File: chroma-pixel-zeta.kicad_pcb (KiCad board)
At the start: 6 copper layers, 76 x 78 mm, 134 parts, among them J1 Micro_SD_Card_Det_Hirose_DM3AT, J10 Conn_01x06_MountingPin, J2 TFT_LCD, J4 USB-C, J5 I2C-STEMMA-QT, J6 BAT, J7 swd, J8 SPKR, J9 UART, SW1 SW_Push, SW2 SW_Push, SW3 SW_Push, SW4 SW_Push, U1 MT25Q, U10 STM32H743ZITx, U11 MT48LC16M16A2P, U5 TPS61169, U6 MAX98357AETE_, U7 CAT24C128, U8 TLV75733PDBV, Y1 25MHz, Y2 32.768KHz

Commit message: Change MCU to STM32H743IIT6
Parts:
- removed U10: STM32H743ZITx, Package_QFP:LQFP-144_20x20mm_P0.5mm
- added U2: STM32H743IITx, Package_QFP:LQFP-176_24x24mm_P0.5mm, F.Cu at (209.2, 83.5)
- moved C10 83.2 mm to (68.8, 75.6)
- moved C21 83.2 mm to (90.7, 86.8)
- moved C24 83.2 mm to (31.8, 99.3)
- moved C27 83.2 mm to (31.8, 110.9)
- moved C28 83.2 mm to (31.8, 116.6)
- moved C29 83.2 mm to (46.1, 80.6)
- moved C35 83.2 mm to (75.8, 104.1)
- moved C42 83.2 mm to (73.4, 73.5)
- moved D5 83.2 mm to (86.2, 51.6)
- moved D6 83.2 mm to (79.2, 51.6)
- moved H2 83.2 mm to (95.6, 52.7)
- moved H3 83.2 mm to (95.6, 123.9)
- moved J10 83.2 mm to (58.1, 52.9)
- moved J2 83.2 mm to (68.5, 36.9)
- moved J5 83.2 mm to (58.0, 122.0)
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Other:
- board size 76 x 78 mm -> 244.9 x 78 mm

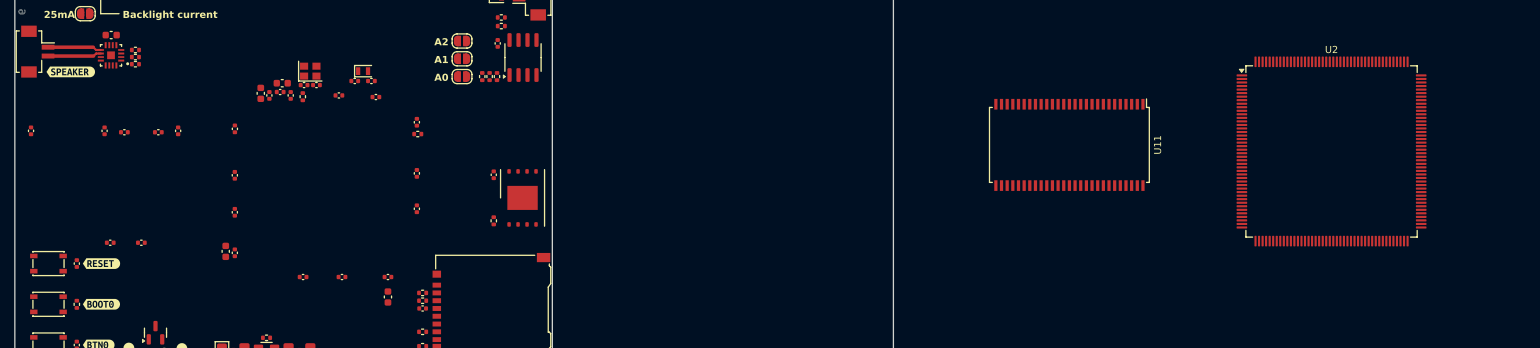
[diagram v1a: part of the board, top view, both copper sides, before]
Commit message: Cleaning schematic, added more independently schematics
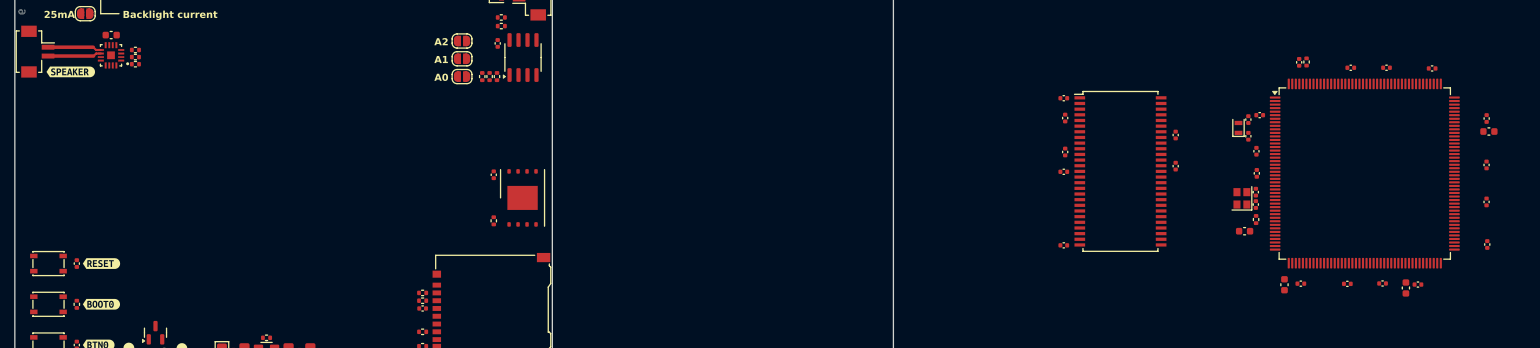
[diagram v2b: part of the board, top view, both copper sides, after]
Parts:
- moved C34 179.4 mm to (231.4, 80.7), turned to 0 degrees
- moved C14 177.0 mm to (231.1, 78.8), turned to -90 degrees
- moved C15 177.0 mm to (231.1, 85.4), turned to -90 degrees
- moved C16 177.0 mm to (231.1, 90.6), turned to -90 degrees
- moved C25 172.0 mm to (231.2, 96.6), turned to -90 degrees
- moved C9 161.6 mm to (221.4, 102.3), turned to 180 degrees
- moved C37 151.0 mm to (187.2, 85.6), turned to -90 degrees
- moved C19 147.3 mm to (202.5, 102.3), turned to -90 degrees
- moved C38 147.0 mm to (187.2, 81.2), turned to -90 degrees
- moved C1 146.9 mm to (171.3, 96.8), turned to 180 degrees
- moved C17 145.2 mm to (198.6, 83.5)
- moved C8 144.9 mm to (223.4, 71.8), turned to 0 degrees
- moved C35 143.9 mm to (219.7, 102.8)
- moved C6 142.2 mm to (211.4, 102.2)
- moved C5 141.1 mm to (204.9, 102.2)
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
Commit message: Layout SDRAM
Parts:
- removed U11: MT48LC16M16A2P, Package_SO:TSOP-II-54_22.2x10.16mm_P0.8mm
- removed kibuzzard-66417165: G***, kibuzzard-66417165
- removed kibuzzard-66417197: G***, kibuzzard-66417197
- removed kibuzzard-6641D19D: G***, kibuzzard-6641D19D
- removed kibuzzard-6641D1A5: G***, kibuzzard-6641D1A5
- removed kibuzzard-6641D1AA: G***, kibuzzard-6641D1AA
- removed kibuzzard-6641D1B0: G***, kibuzzard-6641D1B0
- removed kibuzzard-6642BE54: G***, kibuzzard-6642BE54
- removed kibuzzard-6642BE6C: G***, kibuzzard-6642BE6C
- removed kibuzzard-6642BE85: G***, kibuzzard-6642BE85
- removed kibuzzard-664329E8: G***, kibuzzard-664329E8
- removed kibuzzard-664329F6: G***, kibuzzard-664329F6
- removed kibuzzard-6644A0DC: G***, kibuzzard-6644A0DC
- removed kibuzzard-6644A120: G***, kibuzzard-6644A120
- removed kibuzzard-6644A126: G***, kibuzzard-6644A126
- added C22: 100n, Capacitor_SMD:C_0402_1005Metric, F.Cu at (181.1, 97.6)
- added J3: Conn_01x10_MountingPin, Connector_FFC-FPC:Hirose_FH12-10S-0.5SH_1x10-1MP_P0.50mm_Horizontal, F.Cu at (120.4, 148.3)
- added R1: 10K, Resistor_SMD:R_0402_1005Metric, F.Cu at (181.1, 91.6)
- added R35: 4K7, Resistor_SMD:R_0402_1005Metric, F.Cu at (133.1, 142.4)
- added R36: 4K7, Resistor_SMD:R_0402_1005Metric, F.Cu at (133.1, 144.4)
- added U10: PCM5102A, Package_SO:TSSOP-20_4.4x6.5mm_P0.65mm, F.Cu at (199.6, 98.7)
- added U4: MT25Q, Package_SON:WSON-8-1EP_8x6mm_P1.27mm_EP3.4x4.3mm, F.Cu at (174.8, 102.0)
- added U9: MT48LC16M16A2P, Package_SO:TSOP-II-54_22.2x10.16mm_P0.8mm, F.Cu at (142.3, 128.5)
- J10: value Conn_01x06_MountingPin -> Conn_01x24_MountingPin; footprint Connector_FFC-FPC:TE_84953-6_1x06-1MP_P1.0mm_Horizontal -> Connector_FFC-FPC:Hirose_FH12-24S-0.5SH_1x24-1MP_P0.50mm_Horizontal
- R31, R32: value 10K -> 2K2
- R5, R6: value 2K2 -> 10K
- moved SW1 207.1 mm to (231.6, 62.6), turned to 90 degrees
- moved SW2 206.6 mm to (231.6, 71.6), turned to 90 degrees
- moved SW3 206.1 mm to (231.6, 80.6), turned to 90 degrees
- moved SW4 205.6 mm to (231.6, 89.6), turned to 90 degrees
- moved H1 203.7 mm to (229.8, 40.9)
- moved C24 193.1 mm to (222.1, 66.4)
- moved C27 193.1 mm to (222.1, 78.0)
- moved C28 193.1 mm to (222.1, 83.7)
- moved R18 193.1 mm to (222.1, 72.2)
- moved H2 164.8 mm to (228.9, 149.5)
- moved J9 158.7 mm to (171.9, 39.8), turned to 180 degrees
- moved D7 153.3 mm to (219.6, 144.5), turned to 90 degrees
- moved JP1 153.3 mm to (164.8, 142.2), turned to 180 degrees
- moved JP2 153.1 mm to (164.8, 138.6), turned to 180 degrees
- moved JP3 153.0 mm to (164.8, 135.1), turned to 180 degrees
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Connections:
- net /Audio/GAIN_SLOT renamed /AUDIO/GAIN_SLOT
- net /Audio/SPK+ renamed /AUDIO/SPK+
- net /Audio/SPK- renamed /AUDIO/SPK-
- net /IO/NRST renamed /MCU/NRST
- net /IO/SWCLK renamed /IO/DBG_SWCLK
- net /IO/SWDIO renamed /IO/DBG_SWDIO
- net /IO/USART1_RX renamed /IO/DBG_RX
- net /IO/USART1_TX renamed /IO/DBG_TX
- net /LCD/HSYNC renamed /LCD/LTDC_HSYNC
- net /LCD/LCD_CLK renamed /LCD/LTDC_CLK
- net /LCD/LCD_DE renamed /LCD/LTDC_DE
- net /LCD/LCD_SPI_CS renamed /LCD/LCD_CS
- net /LCD/VSYNC renamed /LCD/LTDC_VSYNC
- net /MCU/I2S_CK renamed /AUDIO/I2S_CK
- net /MCU/I2S_SDO renamed /AUDIO/I2S_SDO
- net /MCU/I2S_SD_MODE renamed /AUDIO/I2S_SD_MODE
- net /MCU/I2S_WS renamed /AUDIO/I2S_WS
- net /MCU/SD_CLK renamed /MEMORY SD CARD/SD_CLK
- net /MCU/SD_CMD renamed /MEMORY SD CARD/SD_CMD
- net /MCU/SD_DAT0 renamed /MEMORY SD CARD/SD_DAT0
- net /MCU/SD_DAT1 renamed /MEMORY SD CARD/SD_DAT1
- net /MCU/SD_DAT2 renamed /MEMORY SD CARD/SD_DAT2
- net /MCU/SD_DAT3 renamed /MEMORY SD CARD/SD_DAT3
- net /MCU/SHIELD renamed /USB/SHIELD
- net /MCU/USB_D+ renamed /USB/USB_D+
- net /MCU/USB_D- renamed /USB/USB_D-
- J1 pad 9: /MCU/PG13 -> /MEMORY SD CARD/SD_DET
- J10 pad 1: GND -> unconnected-(J10-Pin_1-Pad1)
- J10 pad 2: /LCD/LCD_TP_INT -> unconnected-(J10-Pin_2-Pad2)
- J10 pad 3: /LCD/LCD_TP_RST -> unconnected-(J10-Pin_3-Pad3)
- J10 pad 4: +3V3 -> unconnected-(J10-Pin_4-Pad4)
- J10 pad 5: /LCD/LCD_TP_SCL -> unconnected-(J10-Pin_5-Pad5)
- J10 pad 6: /LCD/LCD_TP_SDA -> unconnected-(J10-Pin_6-Pad6)
- J2 pad 5: /LCD/LCD_SPI_DAT -> /LCD/LCD_SDA
- J2 pad 6: /LCD/LCD_SPI_CLK -> /LCD/LCD_SCL
- J7 pad 8: unconnected-(J7-Pin_8-Pad8) -> /IO/DBG_SWO
- R10 pad 1: /MCU/PG13 -> +3V3
- R10 pad 2: +3V3 -> /MEMORY SD CARD/SD_DET
- R2 pad 2: /MCU/~{NOR_CS} -> /MCU/QUADSPI_BK2_NCS
- R31 pad 1: Net-(JP6-A) -> +3V3
- R31 pad 2: GND -> /MEMORY EEPROM/SDA
- R32 pad 1: Net-(JP5-A) -> +3V3
- R32 pad 2: GND -> /MEMORY EEPROM/SCL
- R33 pad 2: /LCD/LCD_TP_SDA -> /LCD/LCD_TP_SCL
- R34 pad 2: /LCD/LCD_TP_SCL -> /LCD/LCD_TP_SDA
- R5 pad 1: +3V3 -> Net-(JP5-A)
- R5 pad 2: /IO/STEMMA_SCL -> GND
- R6 pad 1: +3V3 -> Net-(JP6-A)
- R6 pad 2: /IO/STEMMA_SDA -> GND
- U1 pad 1: /MCU/~{NOR_CS} -> /MCU/QUADSPI_BK1_NCS
- U1 pad 2: /MCU/NOR_D1 -> /MCU/QUADSPI_BK1_IO1
- U1 pad 3: /MCU/NOR_D2 -> /MCU/QUADSPI_BK1_IO2
- U1 pad 5: /MCU/NOR_D0 -> /MCU/QUADSPI_BK1_IO0
- U1 pad 6: /MCU/NOR_CLK -> /MCU/QUADSPI_CLK
- U1 pad 7: /MCU/NOR_D3 -> /MCU/QUADSPI_BK1_IO3
- U2 pad 104: unconnected-(U2-PD14-Pad104) -> /MCU/SDRAM_DQ0
- U2 pad 105: unconnected-(U2-PD15-Pad105) -> /MCU/SDRAM_DQ1
- U2 pad 106: unconnected-(U2-PG2-Pad106) -> /MCU/SDRAM_ADD12
- U2 pad 108: unconnected-(U2-PG4-Pad108) -> /MEMORY SDRAM/SDRAM_BA0
- U2 pad 109: unconnected-(U2-PG5-Pad109) -> /MEMORY SDRAM/SDRAM_BA1
- U2 pad 112: unconnected-(U2-PG8-Pad112) -> /MEMORY SDRAM/SDRAM_CLK
- U2 pad 140: unconnected-(U2-PC11-Pad140) -> /MCU/QUADSPI_BK2_NCS
- U2 pad 142: unconnected-(U2-PD0-Pad142) -> /MCU/SDRAM_DQ2
- U2 pad 143: unconnected-(U2-PD1-Pad143) -> /MCU/SDRAM_DQ3
- U2 pad 152: unconnected-(U2-PG9-Pad152) -> /MCU/QUADSPI_BK2_IO2
- U2 pad 157: unconnected-(U2-PG14-Pad157) -> /MCU/QUADSPI_BK2_IO3
- U2 pad 16: unconnected-(U2-PF0-Pad16) -> /MCU/SDRAM_ADD0
- U2 pad 160: unconnected-(U2-PG15-Pad160) -> /MEMORY SDRAM/~{SDRAM_CAS}
- U2 pad 161: unconnected-(U2-PB3-Pad161) -> /IO/DBG_SWO
- U2 pad 169: unconnected-(U2-PE0-Pad169) -> /MEMORY SDRAM/SDRAM_LDQM
- U2 pad 17: unconnected-(U2-PF1-Pad17) -> /MCU/SDRAM_ADD1
- U2 pad 170: unconnected-(U2-PE1-Pad170) -> /MEMORY SDRAM/SDRAM_UDQM
- U2 pad 18: unconnected-(U2-PF2-Pad18) -> /MCU/SDRAM_ADD2
- U2 pad 19: unconnected-(U2-PF3-Pad19) -> /MCU/SDRAM_ADD3
- U2 pad 20: unconnected-(U2-PF4-Pad20) -> /MCU/SDRAM_ADD4
- U2 pad 21: unconnected-(U2-PF5-Pad21) -> /MCU/SDRAM_ADD5
- U2 pad 24: unconnected-(U2-PF6-Pad24) -> /MCU/QUADSPI_BK1_IO3
- U2 pad 25: unconnected-(U2-PF7-Pad25) -> /MCU/QUADSPI_BK1_IO2
- U2 pad 26: unconnected-(U2-PF8-Pad26) -> /MCU/QUADSPI_BK1_IO0
- U2 pad 27: unconnected-(U2-PF9-Pad27) -> /MCU/QUADSPI_BK1_IO1
- U2 pad 35: unconnected-(U2-PC3_C-Pad35) -> /MEMORY SDRAM/SDRAM_CKE
- U2 pad 43: unconnected-(U2-PH2-Pad43) -> /MCU/QUADSPI_BK2_IO0
- U2 pad 44: unconnected-(U2-PH3-Pad44) -> /MCU/QUADSPI_BK2_IO1
- U2 pad 53: unconnected-(U2-PA7-Pad53) -> /MEMORY SDRAM/~{SDRAM_WE}
- U2 pad 54: unconnected-(U2-PC4-Pad54) -> /MEMORY SDRAM/~{SDRAM_CS}
- U2 pad 58: unconnected-(U2-PB2-Pad58) -> /MCU/QUADSPI_CLK
- U2 pad 59: unconnected-(U2-PF11-Pad59) -> /MEMORY SDRAM/~{SDRAM_RAS}
- U2 pad 60: unconnected-(U2-PF12-Pad60) -> /MCU/SDRAM_ADD6
- U2 pad 63: unconnected-(U2-PF13-Pad63) -> /MCU/SDRAM_ADD7
- U2 pad 64: unconnected-(U2-PF14-Pad64) -> /MCU/SDRAM_ADD8
- U2 pad 65: unconnected-(U2-PF15-Pad65) -> /MCU/SDRAM_ADD9
- U2 pad 66: unconnected-(U2-PG0-Pad66) -> /MCU/SDRAM_ADD10
- U2 pad 67: unconnected-(U2-PG1-Pad67) -> /MCU/SDRAM_ADD11
- U2 pad 68: unconnected-(U2-PE7-Pad68) -> /MCU/SDRAM_DQ4
- U2 pad 69: unconnected-(U2-PE8-Pad69) -> /MCU/SDRAM_DQ5
- U2 pad 70: unconnected-(U2-PE9-Pad70) -> /MCU/SDRAM_DQ6
- U2 pad 73: unconnected-(U2-PE10-Pad73) -> /MCU/SDRAM_DQ7
- U2 pad 74: unconnected-(U2-PE11-Pad74) -> /MCU/SDRAM_DQ8
- U2 pad 75: unconnected-(U2-PE12-Pad75) -> /MCU/SDRAM_DQ9
- U2 pad 76: unconnected-(U2-PE13-Pad76) -> /MCU/SDRAM_DQ10
- U2 pad 77: unconnected-(U2-PE14-Pad77) -> /MCU/SDRAM_DQ11
- U2 pad 78: unconnected-(U2-PE15-Pad78) -> /MCU/SDRAM_DQ12
- U2 pad 79: unconnected-(U2-PB10-Pad79) -> /MCU/QUADSPI_BK1_NCS
- U2 pad 96: unconnected-(U2-PD8-Pad96) -> /MCU/SDRAM_DQ13
- U2 pad 97: unconnected-(U2-PD9-Pad97) -> /MCU/SDRAM_DQ14
- U2 pad 98: unconnected-(U2-PD10-Pad98) -> /MCU/SDRAM_DQ15
- U7 pad 1: Net-(JP7-A) -> Net-(JP5-A)
- U7 pad 3: Net-(JP5-A) -> Net-(JP7-A)
- U7 pad 5: /IO/STEMMA_SCL -> /MEMORY EEPROM/SDA
- U7 pad 6: /IO/STEMMA_SDA -> /MEMORY EEPROM/SCL
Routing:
- net +3V3: track 0.00 -> 83.4 mm, vias 0 -> 4
- net GND: track 0.00 -> 65.7 mm, vias 0 -> 5
- net Net-(C34-Pad1): track 0.00 -> 8.60 mm
- net /AUDIO/SPK+: track 7.63 -> 0.00 mm
- net /AUDIO/SPK-: track 7.61 -> 0.00 mm
- net Net-(U2-PDR_ON): track 0.00 -> 4.23 mm
- net VBAT: track 0.00 -> 4.00 mm
- removed copper zone on F.Cu, net /USB/SHIELD
- removed copper zone on In4.Cu, net GND
- removed copper zone on F.Cu, net VBUS
- removed copper zone on In2.Cu, net VBUS
- removed copper zone on F.Cu, net VDD
- removed copper zone on In3.Cu, net VDD
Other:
- board size 244.9 x 78 mm -> 183.4 x 116.6 mm
- copper layers 6 -> 4
- board text removed: "1"
- board text removed: "100mA"
- board text removed: "2"
- board text removed: "25mA"
- board text removed: "3"
- board text removed: "4"
- board text removed: "40"
- board text removed: "5"
- board text removed: "50mA"
- board text removed: "6"
- board text removed: "A0"
- board text removed: "A1"
- board text removed: "A2"
- board text removed: "Backlight current"

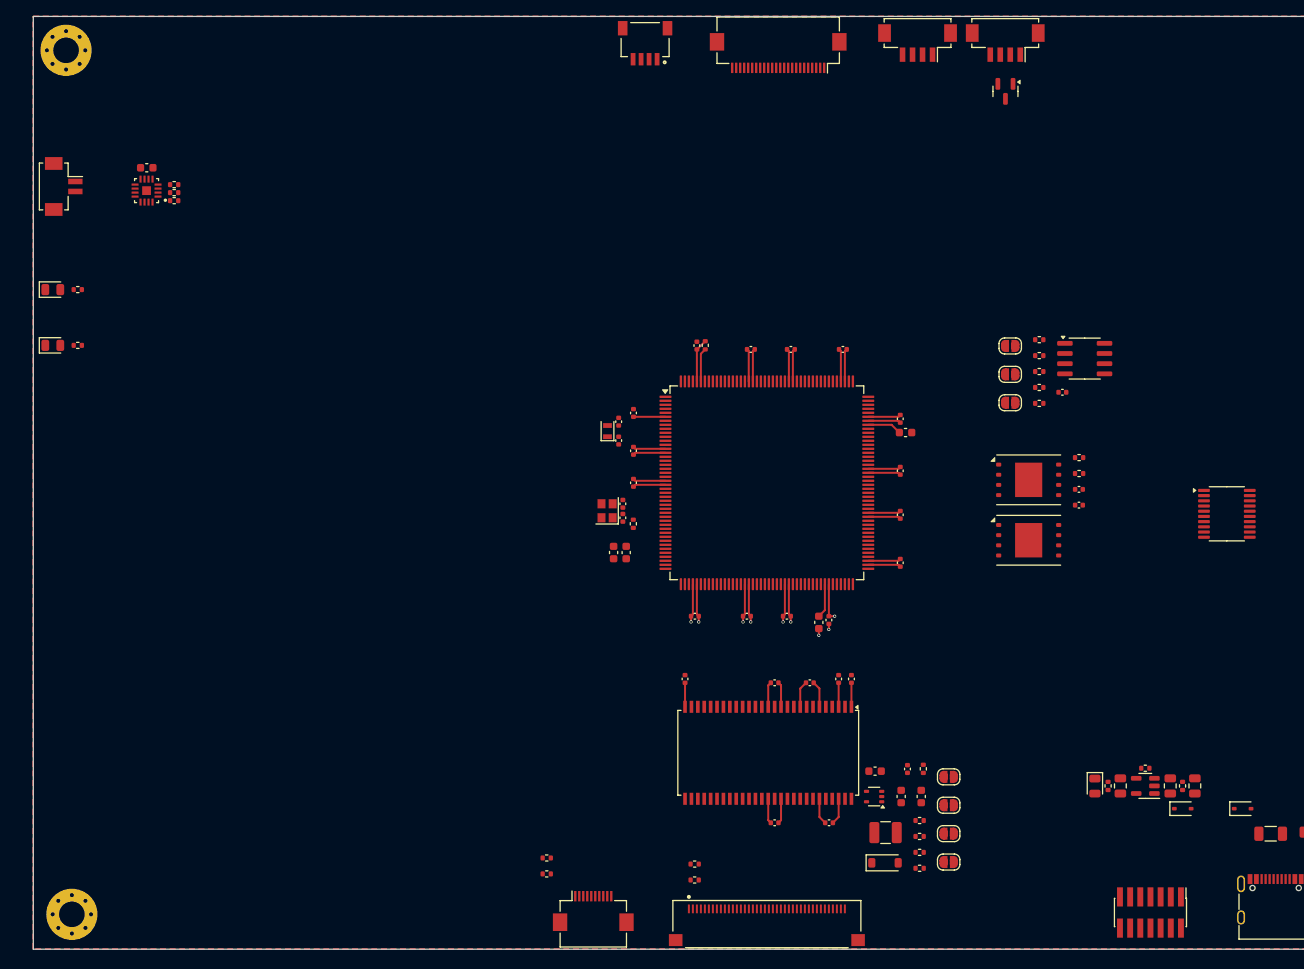
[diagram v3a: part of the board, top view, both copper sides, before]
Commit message: relayout SDRAM
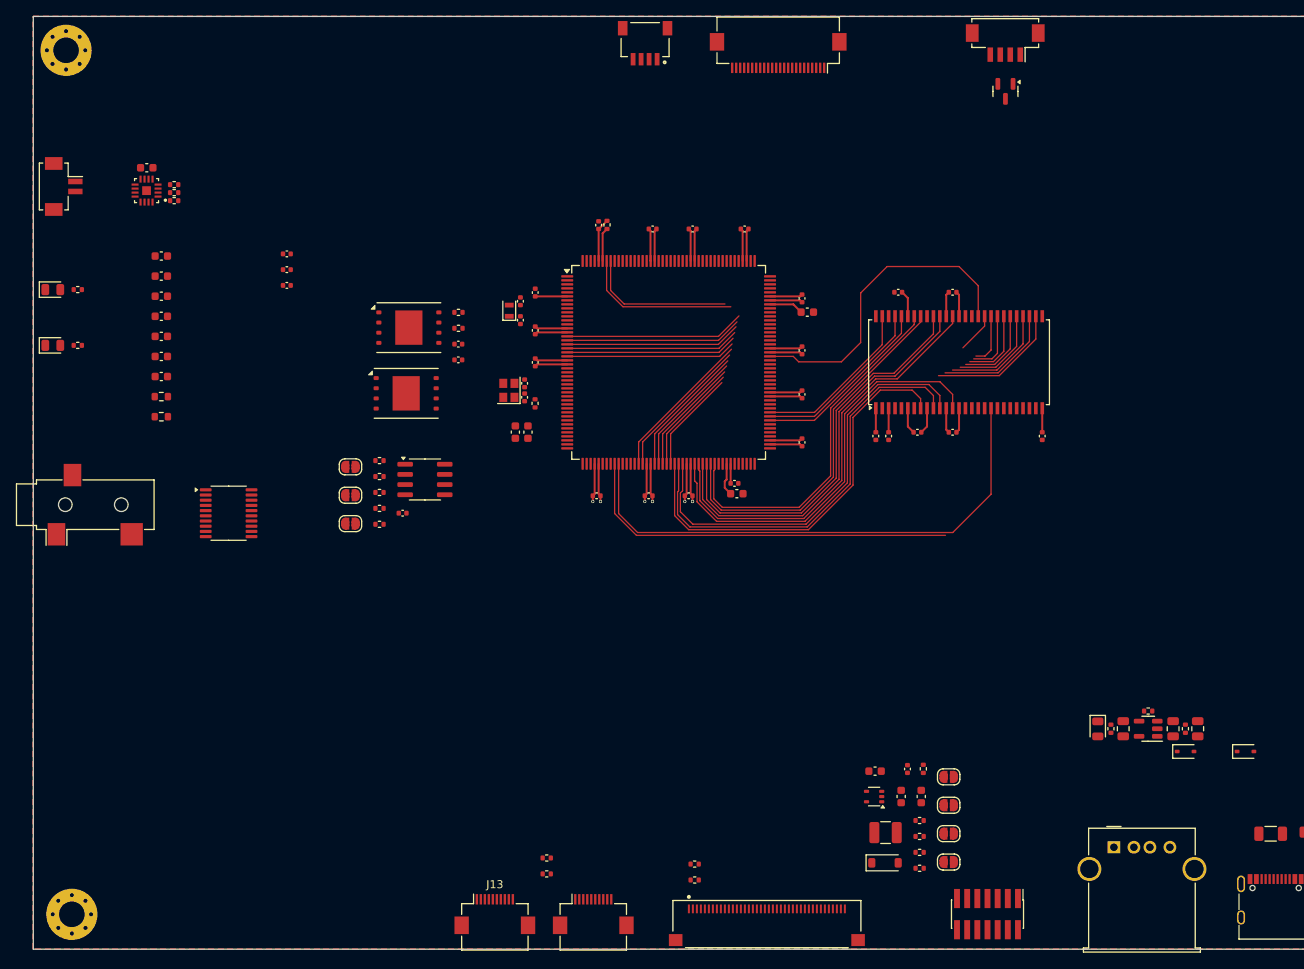
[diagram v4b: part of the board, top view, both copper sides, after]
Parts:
- removed the J9 at (160.9, 39.8)
- added C50: 2.2u, Capacitor_SMD:C_0603_1608Metric, F.Cu at (66.4, 66.4)
- added C51: 2.2u, Capacitor_SMD:C_0603_1608Metric, F.Cu at (66.4, 68.9)
- added C52: 2.2u, Capacitor_SMD:C_0603_1608Metric, F.Cu at (66.4, 71.5)
- added C53: 2.2u, Capacitor_SMD:C_0603_1608Metric, F.Cu at (66.4, 74.0)
- added C54: 10u, Capacitor_SMD:C_0603_1608Metric, F.Cu at (66.4, 76.5)
- added C55: 100n, Capacitor_SMD:C_0402_1005Metric, F.Cu at (82.1, 66.2)
- added C56: 10u, Capacitor_SMD:C_0603_1608Metric, F.Cu at (66.4, 79.0)
- added C57: 100n, Capacitor_SMD:C_0402_1005Metric, F.Cu at (82.1, 68.1)
- added C58: 10u, Capacitor_SMD:C_0603_1608Metric, F.Cu at (66.4, 81.5)
- added C59: 100n, Capacitor_SMD:C_0402_1005Metric, F.Cu at (82.1, 70.1)
- added J11: AudioJack3, Connector_Audio:Jack_3.5mm_CUI_SJ-3523-SMT_Horizontal, F.Cu at (56.9, 97.5)
- added J12: USB_A, Connector_USB:USB_A_Molex_67643_Horizontal, F.Cu at (185.5, 140.3)
- added J13: Conn_01x10_MountingPin, Connector_FFC-FPC:Hirose_FH12-10S-0.5SH_1x10-1MP_P0.50mm_Horizontal, F.Cu at (108.1, 148.7)
- added R37: 470, Resistor_SMD:R_0603_1608Metric, F.Cu at (66.4, 84.0)
- added R38: 470, Resistor_SMD:R_0603_1608Metric, F.Cu at (66.4, 86.5)
- moved U10 124.8 mm to (74.8, 98.6)
- moved C20 83.8 mm to (96.6, 98.6)
- moved JP5 83.8 mm to (90.0, 92.8)
- moved JP6 83.8 mm to (90.0, 96.3)
- moved JP7 83.8 mm to (90.0, 99.9)
- moved R30 83.8 mm to (93.7, 96.0)
- moved R31 83.8 mm to (93.7, 98.0)
- moved R32 83.8 mm to (93.7, 100.0)
- moved R5 83.8 mm to (93.7, 92.0)
- moved R6 83.8 mm to (93.7, 94.0)
- moved U7 83.8 mm to (99.4, 94.4)
- moved U4 81.9 mm to (97.3, 75.4)
- moved C21 79.7 mm to (103.5, 77.4)
- moved C22 79.7 mm to (103.5, 79.4)
- moved R1 79.7 mm to (103.5, 73.5)
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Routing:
- net /MEMORY SDRAM/~{SDRAM_CS}: track 0.00 -> 66.5 mm
- net /MCU/SDRAM_DQ6: track 0.00 -> 53.5 mm
- net /MCU/SDRAM_DQ5: track 0.00 -> 53.2 mm
- net /MCU/SDRAM_DQ8: track 0.00 -> 53.2 mm
- net /MCU/SDRAM_DQ7: track 0.00 -> 52.4 mm
- net /MCU/SDRAM_DQ4: track 0.00 -> 51.8 mm
- net /MCU/SDRAM_DQ9: track 0.00 -> 51.3 mm
- net /MCU/SDRAM_DQ10: track 0.00 -> 49.9 mm
- net /MEMORY SDRAM/~{SDRAM_WE}: track 0.00 -> 48.7 mm
- net /MCU/SDRAM_DQ11: track 0.00 -> 46.7 mm
- net /MCU/SDRAM_DQ12: track 0.00 -> 45.4 mm
- net /MEMORY SDRAM/SDRAM_CLK: track 0.00 -> 39.7 mm
- net /MCU/SDRAM_ADD4: track 0.00 -> 38.4 mm
- net /MCU/SDRAM_ADD5: track 0.00 -> 36.6 mm
- net /MCU/SDRAM_ADD6: track 0.00 -> 31.7 mm
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
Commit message: Finished SDRAM, QSPI Flash, Planning to move to 5 inch orient display dimension
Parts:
- removed J13, J3: Conn_01x10_MountingPin, Connector_FFC-FPC:Hirose_FH12-10S-0.5SH_1x10-1MP_P0.50mm_Horizontal
- added BT1: Battery_Cell, Battery:BatteryHolder_Keystone_2998_1x6.8mm, F.Cu at (66.9, 123.5)
- added C60: 10uF/0805, Capacitor_SMD:C_0805_2012Metric, F.Cu at (188.4, 111.4)
- added C61: 1uF/0805, Capacitor_SMD:C_0805_2012Metric, F.Cu at (188.4, 114.4)
- added C62: 2.2u, Capacitor_SMD:C_0805_2012Metric, F.Cu at (188.4, 117.4)
- added D11: NSR0320MW2T1G, Diode_SMD:D_SOD-323, F.Cu at (195.7, 119.0)
- added D12: GREEN, LED_SMD:LED_0805_2012Metric, F.Cu at (195.7, 116.0)
- added J14: LCD_TP_I2C, Connector_FFC-FPC:TE_84952-6_1x06-1MP_P1.0mm_Horizontal, F.Cu at (110.1, 149.9)
- added J15: LCD_SPI, Connector_FFC-FPC:TE_84952-6_1x06-1MP_P1.0mm_Horizontal, F.Cu at (70.1, 147.5)
- added R39: 100K, Resistor_SMD:R_0402_1005Metric, F.Cu at (192.0, 115.5)
- added R40: 10K, Resistor_SMD:R_0402_1005Metric, F.Cu at (192.0, 117.5)
- added R41: 2K2, Resistor_SMD:R_0402_1005Metric, F.Cu at (192.0, 119.5)
- added U11: TLV75733PDBV, Package_TO_SOT_SMD:SOT-23-5, F.Cu at (193.2, 112.3)
- C50, C51, C52, C53: footprint Capacitor_SMD:C_0603_1608Metric -> Capacitor_SMD:C_0805_2012Metric
- moved H3 409.5 mm to (451.1, 142.5), turned to 0 degrees
- moved H4 406.5 mm to (451.1, 56.5), turned to 90 degrees
- moved C16 255.4 mm to (401.4, 98.6)
- moved C1 255.4 mm to (431.5, 103.5)
- moved C13 255.4 mm to (387.8, 77.6)
- moved C14 255.4 mm to (401.4, 86.3)
- moved C15 255.4 mm to (401.4, 92.8)
- moved C2 255.4 mm to (420.3, 103.1)
- moved C25 255.4 mm to (401.4, 104.3)
- moved C26 255.4 mm to (367.2, 103.0)
- moved C29 255.4 mm to (412.3, 103.5)
- moved C36 255.4 mm to (420.3, 85.6)
- moved C37 255.4 mm to (413.5, 85.6)
- moved C5 255.4 mm to (387.3, 111.0)
- moved C8 255.4 mm to (394.3, 77.6)
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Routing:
- net /MEMORY SDRAM/~{SDRAM_CAS}: track 0.00 -> 56.2 mm, vias 0 -> 2
- net /MEMORY SDRAM/SDRAM_CKE: track 5.07 -> 59.9 mm, vias 0 -> 2
- net /MCU/QUADSPI_BK2_IO2: track 0.00 -> 50.5 mm
- net /MCU/QUADSPI_BK2_IO0: track 0.00 -> 47.2 mm
- net /MCU/QUADSPI_BK2_IO3: track 0.00 -> 46.8 mm
- net /MEMORY SDRAM/SDRAM_LDQM: track 18.7 -> 64.8 mm, vias 0 -> 2
- net /MCU/SDRAM_DQ3: track 0.00 -> 44.4 mm, vias 0 -> 2
- net /MCU/SDRAM_DQ2: track 0.00 -> 42.0 mm, vias 0 -> 2
- net /MCU/QUADSPI_BK2_IO1: track 0.00 -> 42.0 mm
- net /MCU/QUADSPI_CLK: track 0.00 -> 41.6 mm, vias 0 -> 2
- net /MCU/SDRAM_ADD3: track 21.8 -> 62.2 mm, vias 0 -> 2
- net /MCU/SDRAM_ADD10: track 13.8 -> 53.5 mm, vias 0 -> 2
- net /MCU/SDRAM_ADD2: track 22.0 -> 61.6 mm, vias 0 -> 2
- net /MCU/SDRAM_ADD1: track 22.2 -> 61.0 mm, vias 0 -> 2
- net /MCU/SDRAM_ADD0: track 22.5 -> 60.4 mm, vias 0 -> 2
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- added copper zone on B.Cu, net GND
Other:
- board size 183.4 x 116.6 mm -> 292.9 x 116.6 mm

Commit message: Move to 5 inch dimension
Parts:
- moved C1 238.4 mm to (193.3, 93.0)
- moved C10 238.4 mm to (137.9, 66.6)
- moved C12 238.4 mm to (144.6, 67.1)
- moved C13 238.4 mm to (149.6, 67.1)
- moved C14 238.4 mm to (163.3, 75.8)
- moved C15 238.4 mm to (163.3, 82.3)
- moved C16 238.4 mm to (163.3, 88.0)
- moved C2 238.4 mm to (182.1, 92.5)
- moved C25 238.4 mm to (163.3, 93.8)
- moved C26 238.4 mm to (129.0, 92.5)
- moved C29 238.4 mm to (174.1, 93.0)
- moved C36 238.4 mm to (182.1, 75.0)
- moved C37 238.4 mm to (175.3, 75.0)
- moved C39 238.4 mm to (128.6, 86.4)
- moved C40 238.4 mm to (128.6, 88.1)
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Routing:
- net /MCU/QUADSPI_BK1_NCS: track 1.61 -> 59.9 mm, vias 0 -> 2
- net /MCU/QUADSPI_BK2_NCS: track 1.61 -> 56.6 mm, vias 0 -> 2
- net /MCU/QUADSPI_BK1_IO3: track 17.4 -> 48.0 mm
- net /MCU/QUADSPI_BK1_IO0: track 18.3 -> 48.0 mm
- net /MCU/QUADSPI_BK1_IO1: track 24.3 -> 44.9 mm
- net /MCU/QUADSPI_BK1_IO2: track 28.0 -> 44.9 mm
- net /MCU/QUADSPI_CLK: track 41.6 -> 53.7 mm
- net /MCU/QUADSPI_BK2_IO1: track 42.0 -> 48.0 mm
- net /MCU/QUADSPI_BK2_IO2: track 50.5 -> 44.9 mm, vias 0 -> 2
- net GND: track 79.0 -> 75.5 mm, vias 22 -> 34
- net +3V3: track 95.7 -> 97.9 mm, vias 19 -> 22
- net /MCU/QUADSPI_BK2_IO3: track 46.8 -> 44.9 mm, vias 0 -> 2
- net /MCU/SDRAM_DQ5: track 53.2 -> 52.0 mm
- net /MCU/SDRAM_DQ4: track 51.8 -> 50.5 mm
- net /MCU/SDRAM_DQ7: track 52.4 -> 51.2 mm
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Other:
- board size 292.9 x 116.6 mm -> 138 x 93.2 mm
